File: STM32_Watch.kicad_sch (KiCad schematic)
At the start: 32 parts, among them J1 USB_C_Receptacle_PowerOnly_6P, U1 STM32L031K6Ux, U2 BQ21040DBV, U3 TPS78233DDC, X1 32.768k

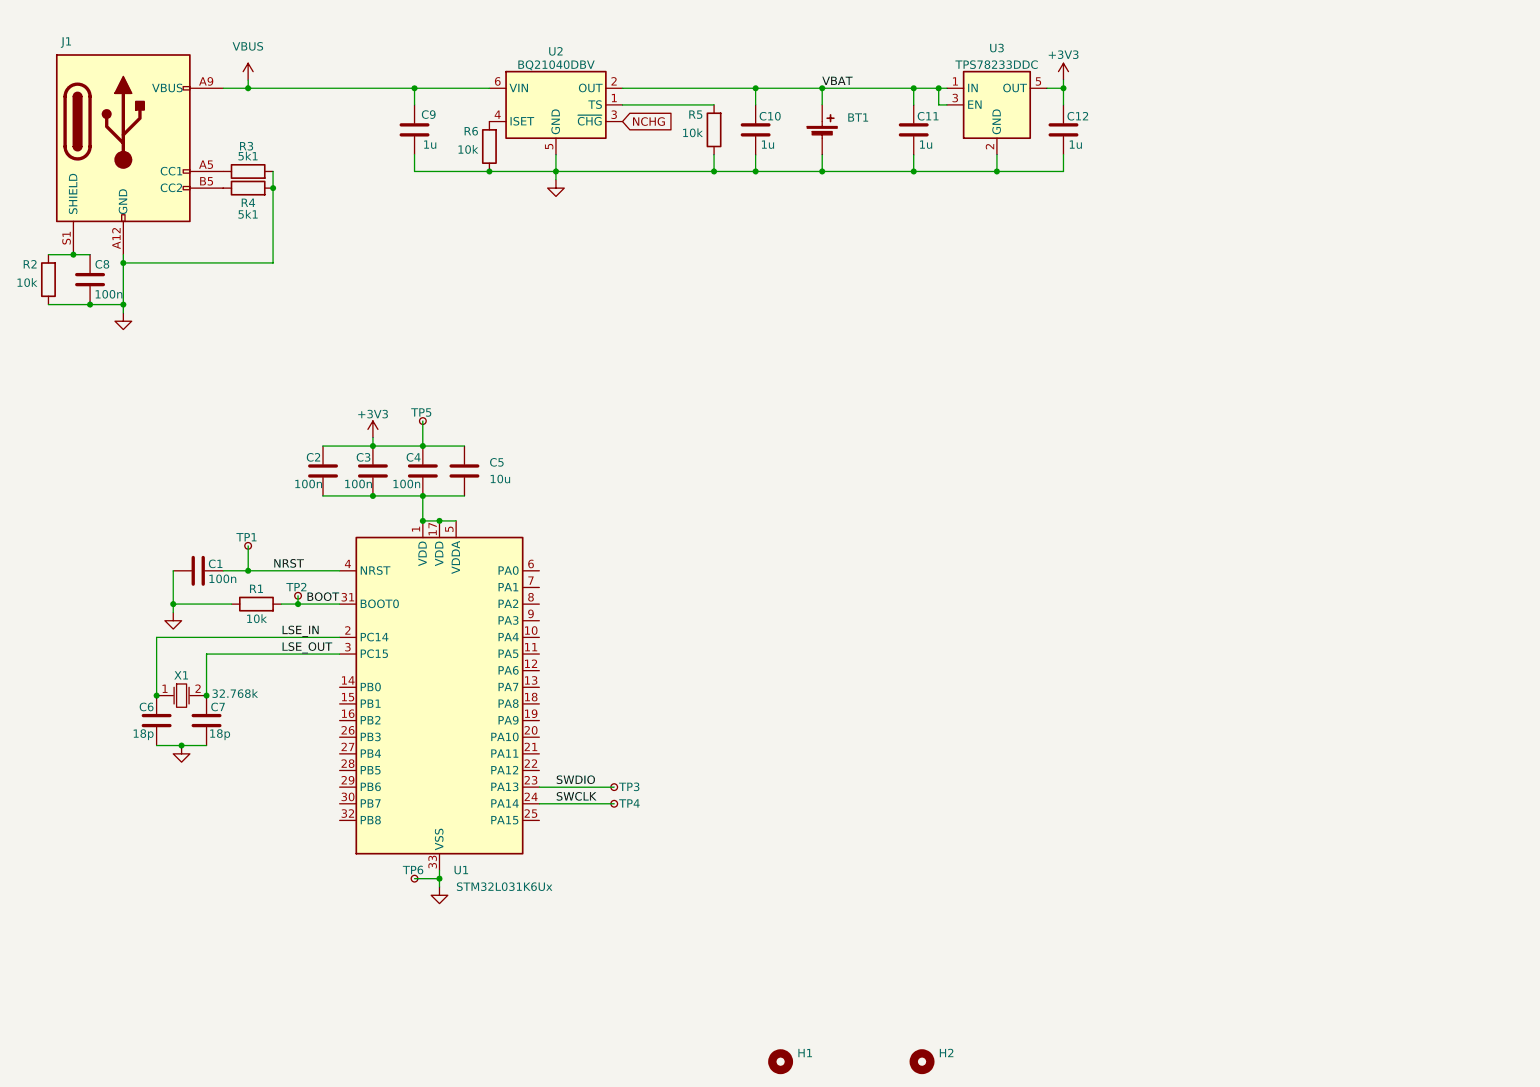
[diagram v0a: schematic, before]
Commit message: Li-po & usb charging -> CR2032 added magnetometer
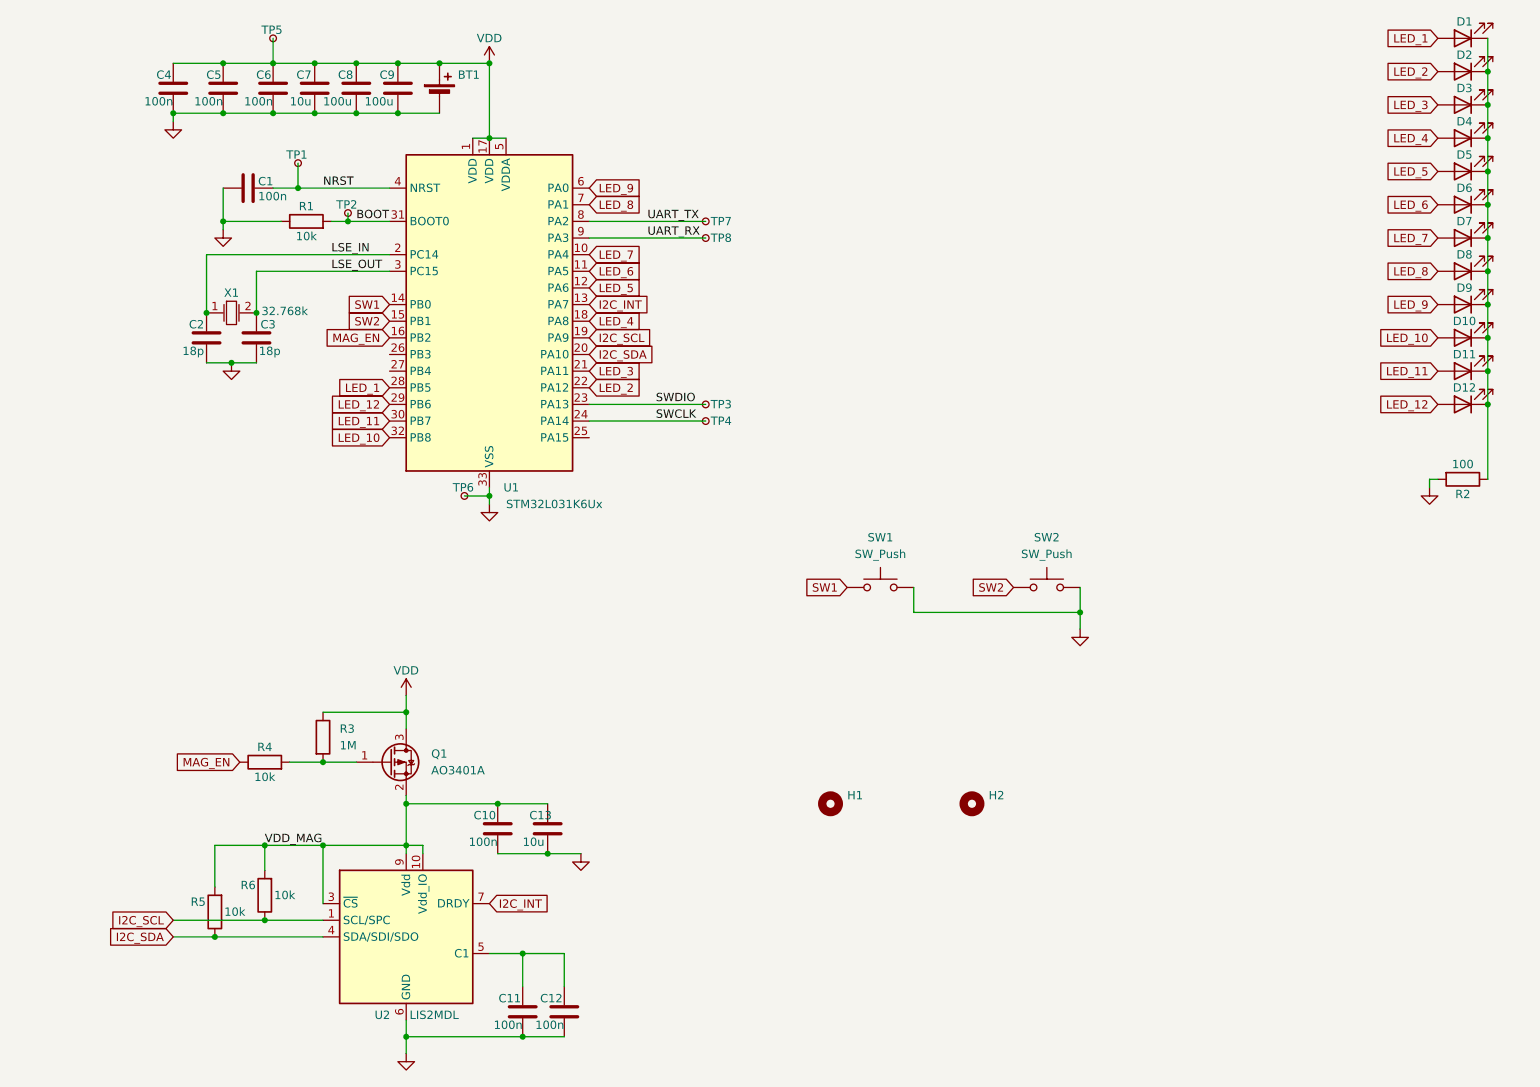
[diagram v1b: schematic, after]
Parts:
- removed J1: USB_C_Receptacle_PowerOnly_6P, symbol Connector:USB_C_Receptacle_PowerOnly_6P
- removed U2: BQ21040DBV, Package_TO_SOT_SMD:SOT-23-6, symbol Battery_Management:BQ21040DBV
- removed U3: TPS78233DDC, Package_TO_SOT_SMD:SOT-23-5, symbol Regulator_Linear:TPS78233DDC
- added C13: 10u, Capacitor_SMD:C_0805_2012Metric, symbol Device:C
- added D1, D10, D11, D12, D2, D3, D4, D5, D6, D7, D8, D9: LED, LED_SMD:LED_0603_1608Metric, symbol Device:LED
- added Q1: AO3401A, Package_TO_SOT_SMD:SOT-23, symbol Transistor_FET:AO3401A
- added SW1, SW2: SW_Push, STM32_Watch:SHOU_HAN_TS24CA, symbol Switch:SW_Push
- added TP7, TP8: TestPoint_Small, TestPoint:TestPoint_Pad_D1.0mm, symbol Connector:TestPoint_Small
- added U2: LIS2MDL, Package_LGA:LGA-12_2x2mm_P0.5mm, symbol Sensor_Magnetic:LIS2MDL
- C10, C11, C12: value 1u -> 100n; LCSC C15849 -> C14663
- C8: value 100n -> 100u; footprint Capacitor_SMD:C_0603_1608Metric -> Capacitor_SMD:C_1206_3216Metric; LCSC C14663 -> C15008
- C9: value 1u -> 100u; footprint Capacitor_SMD:C_0603_1608Metric -> Capacitor_SMD:C_1206_3216Metric; LCSC C15849 -> C15008
- H1, H2: footprint stm8_watch:StapsConnection_20mm -> STM32_Watch:StrapsConnection_20mm
- R2: value 10k -> 100; LCSC C98220 -> C105588
- R3: value 5k1 -> 1M; LCSC C2907044 -> C105578
- R4: value 5k1 -> 10k; LCSC C2907044 -> C98220
- X1: footprint stm8_watch:Crystal_SMD_3215-2pin_3.2x1.5mm -> STM32_Watch:Crystal_SMD_3215-2pin_3.2x1.5mm
- renumbered C6 to C2, C7 to C3, C2 to C4, C3 to C5, C4 to C6, C5 to C7
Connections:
- net VBUS is gone; now on net VDD: C9.1
- net GND: now also C4.2, C5.2, C6.2, C7.2, R2.2, C13.2, SW1.2, SW2.2, U2.6 (GND), U2.8 (GND); no longer R2.1, R3.2, R4.2, R5.1, R6.1
- net VDD_MAG: now reaches R5.2
- net VDD_MAG: now also C10.1, R6.2, C13.1, Q1.2 (S), U2.10 (Vdd_IO), U2.3 (~{CS}), U2.9 (Vdd)
- net VDD: now reaches R3.1
- net VDD: now also BT1.1 (+), C4.1, C5.1, C6.1, C7.1, C8.1, TP5.1, U1.1 (VDD), U1.17 (VDD), U1.5 (VDDA), Q1.3 (D)
- net MAG_EN: now reaches R4.1
- net MAG_EN: now also U1.16 (PB2)
- net LED_7: now reaches U1.10 (PA4)
- net LED_7: now also D7.2 (A)
- net LED_6: now reaches U1.11 (PA5)
- net LED_6: now also D6.2 (A)
- net LED_5: now reaches U1.12 (PA6)
- net LED_5: now also D5.2 (A)
- net I2C_INT: now reaches U1.13 (PA7)
- net I2C_INT: now also U2.7 (DRDY)
- net SW1: now reaches U1.14 (PB0)
- net SW1: now also SW1.1
- net SW2: now reaches U1.15 (PB1)
- net SW2: now also SW2.1
- net LED_4: now reaches U1.18 (PA8)
- net LED_4: now also D4.2 (A)
- net I2C_SCL: now reaches U1.19 (PA9)
- net I2C_SCL: now also R6.1, U2.1 (SCL/SPC)
- net I2C_SDA: now reaches U1.20 (PA10)
- net I2C_SDA: now also R5.1, U2.4 (SDA/SDI/SDO)
- net LED_3: now reaches U1.21 (PA11)
- net LED_3: now also D3.2 (A)
- net LED_2: now reaches U1.22 (PA12)
- net LED_2: now also D2.2 (A)
- net LED_1: now reaches U1.28 (PB5)
- net LED_1: now also D1.2 (A)
- net LED_12: now reaches U1.29 (PB6)
- net LED_12: now also D12.2 (A)
- net LED_11: now reaches U1.30 (PB7)
- net LED_11: now also D11.2 (A)
- net LED_10: now reaches U1.32 (PB8)
- net LED_10: now also D10.2 (A)
- net LED_9: now reaches U1.6 (PA0)
- net LED_9: now also D9.2 (A)
- net LED_8: now reaches U1.7 (PA1)
- net LED_8: now also D8.2 (A)
- net UART_TX: now reaches U1.8 (PA2)
- net UART_TX: now also TP7.1
- net UART_RX: now reaches U1.9 (PA3)
- net UART_RX: now also TP8.1
- removed net +3V3: C12.1, C4.1, C5.1, C6.1, C7.1, TP5.1
- removed net VBAT: BT1.1 (+), C10.1, C11.1
- new net: D1.1 (K), D10.1 (K), D11.1 (K), D12.1 (K), D2.1 (K), D3.1 (K), D4.1 (K), D5.1 (K), D6.1 (K), D7.1 (K), D8.1 (K), D9.1 (K), R2.1
- new net: Q1.1 (G), R3.2, R4.2
- new net: C11.1, C12.1, U2.5 (C1)
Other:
- moved on the sheet: BT1, C1, C2, C3, C4, C5, C6, C7, H1, H2, R1, TP1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

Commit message: Added net lables & ERC fixes
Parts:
- X1: footprint STM32_Watch:Crystal_SMD_3215-2pin_3.2x1.5mm -> Crystal:Crystal_SMD_3215-2Pin_3.2x1.5mm; symbol stm8_watch:EPSON_Q13FC13500004 -> STM32_Watch:Crystal-SMD3215-2P; LCSC C32346 -> C5120559
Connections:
- no-connect marks 0 -> 3
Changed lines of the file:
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@@
 	)
 	(junction
+		(at 72.39 153.67)
+		(diameter 0)
+		(color 0 0 0 0)
+	)
+	(junction
 		(at 67.31 153.67)
 		(diameter 0)
@@
 		(color 0 0 0 0)
 	)
+	(no_connect
+		(at 77.47 81.28)
+	)
+	(no_connect
+		(at 107.95 91.44)
+	)
+	(no_connect
+		(at 77.47 78.74)
+	)
 	(wire
 		(pts
@@
 	(wire
 		(pts
-			(xy 67.31 153.67) (xy 80.01 153.67)
+			(xy 67.31 153.67) (xy 72.39 153.67)
 		)
 		(stroke
@@
 	(wire
 		(pts
+			(xy 72.39 153.67) (xy 80.01 153.67)
+		)
+		(stroke
+			(width 0)
+			(type default)
+		)
+	)
+	(wire
+		(pts
 			(xy 67.31 140.97) (xy 72.39 140.97)
 		)
@@
 	)
 	(symbol
+		(lib_id "power:PWR_FLAG")
+		(at 92.71 34.29 270)
+		(unit 1)
+		(exclude_from_sim no)
+		(in_bom yes)
+		(on_board yes)
+		(dnp no)
+		(fields_autoplaced yes)
+		(property "Reference" "#FLG01"
+			(at 94.615 34.29 0)
+			(effects
+				(font
+					(size 1.27 1.27)
+				)
+				(hide yes)
+			)
+		)
+		(property "Value" "PWR_FLAG"
+			(at 96.52 34.2899 90)
+			(effects
+				(font
+					(size 1.27 1.27)
+				)
+				(justify left)
+			)
+		)
+		(property "Footprint" ""
+			(at 92.71 34.29 0)
+			(effects
+				(font
+					(size 1.27 1.27)
+				)
+				(hide yes)
+			)
+		)
+		(property "Datasheet" "~"
+			(at 92.71 34.29 0)
+			(effects
+				(font
+					(size 1.27 1.27)
+				)
+				(hide yes)
+			)
+		)
+		(property "Description" "Special symbol for telling ERC where power comes from"
+			(at 92.71 34.29 0)
+			(effects
+				(font
+					(size 1.27 1.27)
+				)
+				(hide yes)
+			)
+		)
+		(pin "1"
+		)
+		(instances
+			(project ""
+				(path "/1b502511-4b9c-43d1-bc6f-3ad66e0f6a7c"
+					(reference "#FLG01")
+					(unit 1)
+				)
+			)
+		)
+	)
+	(symbol
 		(lib_id "power:GND")
 		(at 53.34 80.01 0)
@@
 		(dnp no)
 		(property "Reference" "U1"
-			(at 94.8533 99.06 0)
+			(at 96.6313 44.45 0)
 			(effects
 				(font
@@
 		)
 		(property "Value" "STM32L031K6Ux"
-			(at 95.25 101.6 0)
+			(at 97.028 46.99 0)
 			(effects
 				(font
@@
 	)
 	(symbol
+		(lib_id "power:PWR_FLAG")
+		(at 72.39 153.67 0)
+		(unit 1)
+		(exclude_from_sim no)
+		(in_bom yes)
+		(on_board yes)
+		(dnp no)
+		(fields_autoplaced yes)
+		(property "Reference" "#FLG03"
+			(at 72.39 151.765 0)
+			(effects
+				(font
+					(size 1.27 1.27)
+				)
+				(hide yes)
+			)
+		)
+		(property "Value" "PWR_FLAG"
+			(at 72.39 148.59 0)
+			(effects
+				(font
+					(size 1.27 1.27)
+				)
+			)
+		)
+		(property "Footprint" ""
+			(at 72.39 153.67 0)
+			(effects
+				(font
+					(size 1.27 1.27)
+				)
+				(hide yes)
+			)
+		)
+		(property "Datasheet" "~"
+			(at 72.39 153.67 0)
+			(effects
+				(font
+					(size 1.27 1.27)
+				)
+				(hide yes)
+			)
+		)
+		(property "Description" "Special symbol for telling ERC where power comes from"
+			(at 72.39 153.67 0)
+			(effects
+				(font
+					(size 1.27 1.27)
+				)
+				(hide yes)
+			)
+		)
+		(pin "1"
+		)
+		(instances
+			(project ""
+				(path "/1b502511-4b9c-43d1-bc6f-3ad66e0f6a7c"
+					(reference "#FLG03")
+					(unit 1)
+				)
+			)
+		)
+	)
+	(symbol
 		(lib_id "Connector:TestPoint_Small")
 		(at 63.5 49.53 0)
@@
 	)
 	(symbol
+		(lib_id "power:PWR_FLAG")
+		(at 92.71 100.33 270)
+		(unit 1)
+		(exclude_from_sim no)
+		(in_bom yes)
+		(on_board yes)
+		(dnp no)
+		(fields_autoplaced yes)
+		(property "Reference" "#FLG02"
+			(at 94.615 100.33 0)
+			(effects
+				(font
+					(size 1.27 1.27)
+				)
+				(hide yes)
+			)
+		)
+		(property "Value" "PWR_FLAG"
+			(at 96.52 100.3299 90)
+			(effects
+				(font
+					(size 1.27 1.27)
+				)
+				(justify left)
+			)
+		)
+		(property "Footprint" ""
+			(at 92.71 100.33 0)
+			(effects
+				(font
+					(size 1.27 1.27)
+				)
+				(hide yes)
+			)
+		)
+		(property "Datasheet" "~"
+			(at 92.71 100.33 0)
+			(effects
+				(font
+					(size 1.27 1.27)
+				)
+				(hide yes)
+			)
+		)
+		(property "Description" "Special symbol for telling ERC where power comes from"
+			(at 92.71 100.33 0)
+			(effects
+				(font
+					(size 1.27 1.27)
+				)
+				(hide yes)
+			)
+		)
+		(pin "1"
+		)
+		(instances
+			(project "STM32_Watch"
+				(path "/1b502511-4b9c-43d1-bc6f-3ad66e0f6a7c"
+					(reference "#FLG02")
+					(unit 1)
+				)
+			)
+		)
+	)
+	(symbol
 		(lib_id "power:GND")
 		(at 106.68 154.94 0)
@@
 	)
 	(symbol
-		(lib_id "stm8_watch:EPSON_Q13FC13500004")
+		(lib_id "STM32_Watch:Crystal-SMD3215-2P")
 		(at 53.34 72.39 0)
 		(unit 1)
@@
 			)
 		)
-		(property "Footprint" "STM32_Watch:Crystal_SMD_3215-2pin_3.2x1.5mm"
+		(property "Footprint" "Crystal:Crystal_SMD_3215-2Pin_3.2x1.5mm"
 			(at 53.34 72.39 0)
 			(effects
@@
 			)
 		)
-		(property "LCSC" "C32346"
+		(property "LCSC" "C5120559"
 			(at 53.34 72.39 0)
 			(effects

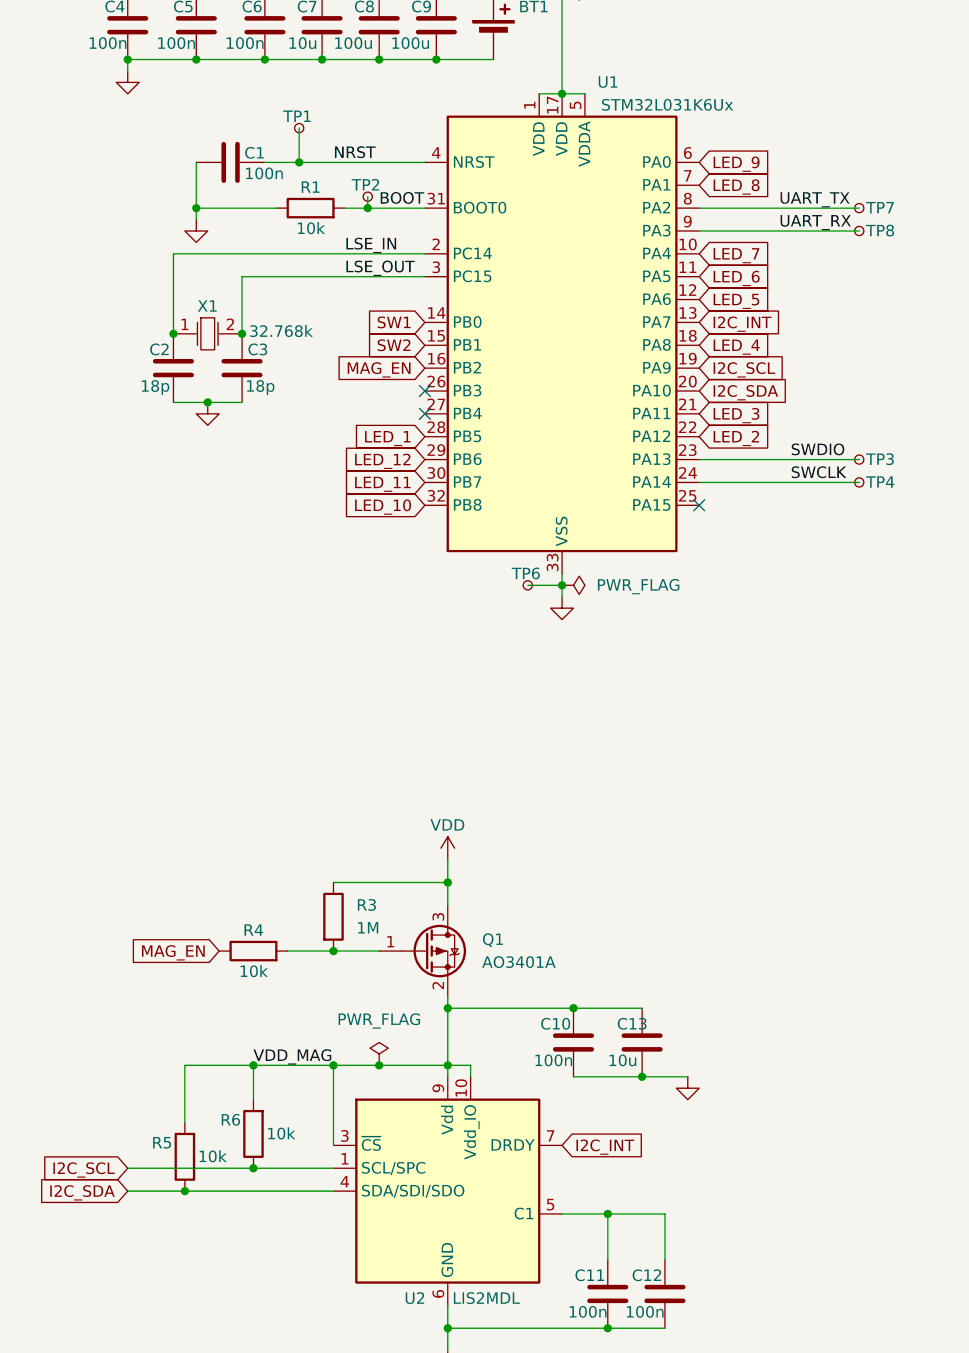
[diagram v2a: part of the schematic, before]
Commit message: Added ALSENS for ambient light measurments
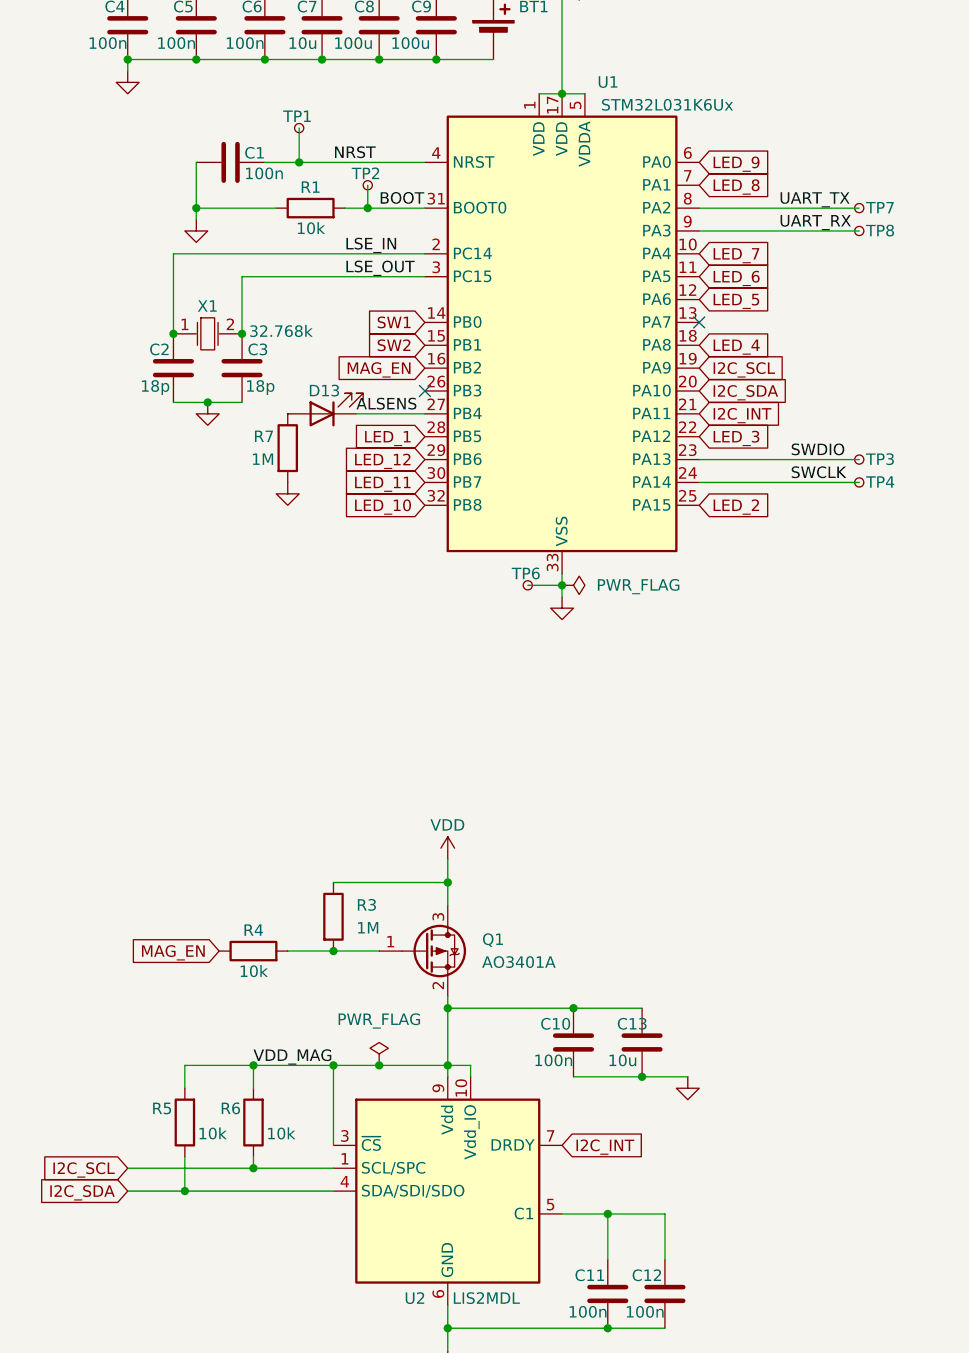
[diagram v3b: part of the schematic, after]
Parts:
- added D13: LED, LED_SMD:LED_0603_1608Metric, symbol Device:LED
- added R7: 1M, Resistor_SMD:R_0603_1608Metric, symbol Device:R
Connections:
- net GND: now also R7.2
- net I2C_INT: now also U1.21 (PA11); no longer U1.13 (PA7)
- net LED_2: now also U1.25 (PA15); no longer U1.22 (PA12)
- net LED_3: now also U1.22 (PA12); no longer U1.21 (PA11)
- net ALSENS: now reaches U1.27 (PB4)
- net ALSENS: now also D13.1 (K)
- new net: D13.2 (A), R7.1
- no-connect marks 3 -> 2
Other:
- moved on the sheet: R5, R6, TP2
